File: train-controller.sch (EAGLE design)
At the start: 19 parts, among them IC1 MCP4131, IC2 L272, Q1 2n3906, Q2 2n2222

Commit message: board v2, adding readme and license
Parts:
- removed 5V: M02, custom-parts:M02
- removed BOOST: M03, custom-parts:M03
- removed R6: 1k, SparkFun-Resistors:1KOHM-1/4W-5%(PTH)
- added AUX: M02, custom-parts:M02
- added POW: M03, custom-parts:M03
- CTL: value M02 -> M03; device custom-parts:M02 -> custom-parts:M03
- Q1: value 2n3906 -> BC838
- R2: value 2.7k -> 1k
- SERIAL: value M03 -> M02; device custom-parts:M03 -> custom-parts:M02
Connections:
- removed net 5V-EN: BOOST.P$1, Q1.C
- removed net N$2: IC1.A, R2.1
- new net 12V-EN: AUX.P$1, IC2.V+, Q1.C
- net 12V: now also POW.P$2, Q1.E; no longer BOOST.P$3, IC2.V+
- net 5V: now also IC1.B, POW.P$1; no longer 5V.P$1, Q1.E, R2.2
- net CS: now also CTL.P$1; no longer SERIAL.P$3
- net DIR: now also CTL.P$3, R5.1; no longer CTL.P$2, R6.1
- net EN: now also CTL.P$2, R4.2; no longer CTL.P$1, R5.2
- net GND: now also AUX.P$2, IC1.A, POW.P$3, R3.2; no longer 5V.P$2, BOOST.P$2, IC1.B, R4.2
- net N$1: now also R4.1; no longer R5.1
- net N$3: now also R2.1; no longer R4.1
- net N$6: now also R5.2; no longer R6.2
- net POW: now also R2.2; no longer R3.2
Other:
- moved on the sheet: R2, R3, R4, R5

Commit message: addressing several items from the bug/feature list
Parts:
- removed Q2: 2n2222, custom-parts:TRANSISTOR_NPNTO92
- added D1: (no value), SparkFun-DiscreteSemi:DIODE1N4148
- added Q3: BC638, custom-parts:TRANSISTOR_PNPTO92
- Q1: value BC838 -> BC638
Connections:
- removed net N$5: Q2.C, S1.-
- new net N$2: D1.C, Q3.C, S1.+
- net 12V: now also POW.P$3; no longer POW.P$2
- net 5V: now also Q3.E; no longer S1.+
- net EN: now also R4.1; no longer R4.2
- net GND: now also D1.A, M(V).P$1, POW.P$2, S1.-; no longer M(V).P$2, POW.P$3, Q2.E
- net N$1: now also R4.2; no longer R4.1
- net N$6: now also Q3.B; no longer Q2.B
- net POW: now also M(V).P$2; no longer M(V).P$1
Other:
- moved on the sheet: M(I), M(V), R4, R5

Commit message: adding controller board
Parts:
- R3: value 1k -> -VAR-
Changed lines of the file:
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@@
 <part name="R4" library="SparkFun-Resistors" deviceset="1KOHM-1/4W-5%(PTH)" device="" value="1k"/>
 <part name="R2" library="SparkFun-Resistors" deviceset="1KOHM-1/4W-5%(PTH)" device="" value="1k"/>
-<part name="R3" library="SparkFun-Resistors" deviceset="1KOHM-1/4W-5%(PTH)" device="" value="1k"/>
+<part name="R3" library="SparkFun-Resistors" deviceset="1KOHM-1/4W-5%(PTH)" device="" value="-VAR-"/>
 <part name="R5" library="SparkFun-Resistors" deviceset="1KOHM-1/4W-5%(PTH)" device="" value="1k"/>
 <part name="S1" library="custom-parts" deviceset="EC2-5NU" device="" value="EC2-5NU"/>

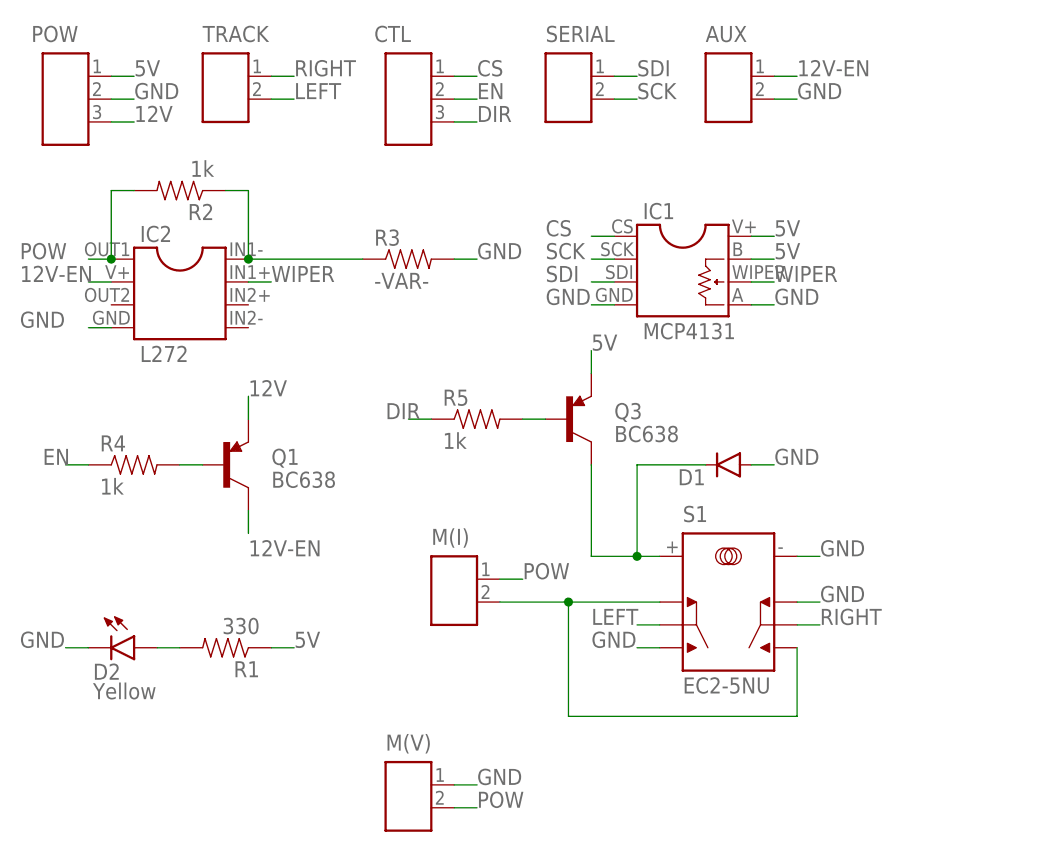
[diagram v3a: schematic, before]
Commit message: getting close to final v2 board, swapping out connectors for molex kk
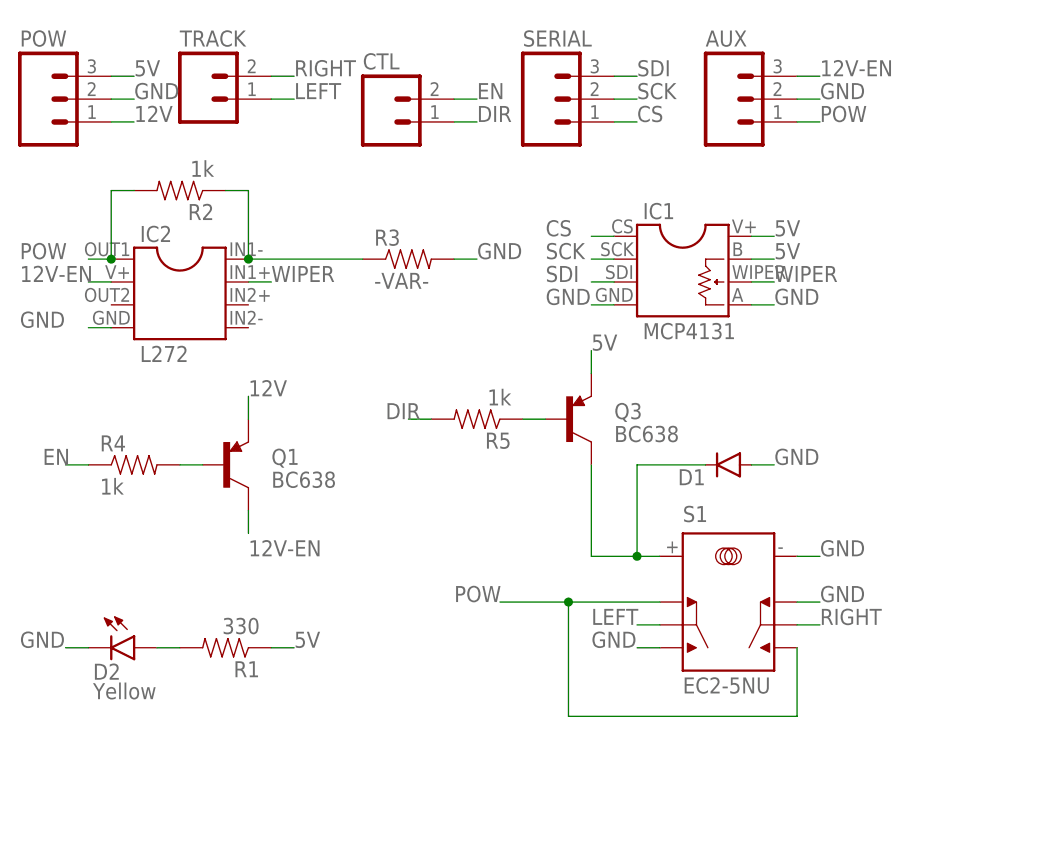
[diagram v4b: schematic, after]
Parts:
- removed M(I), M(V): M02, custom-parts:M02
- AUX, SERIAL: value M02 -> (none); device custom-parts:M02 -> SparkFun-Connectors:M03PTH
- CTL: value M03 -> (none); device custom-parts:M03 -> SparkFun-Connectors:M02PTH
- POW: value M03 -> (none); device custom-parts:M03 -> SparkFun-Connectors:M03PTH
- TRACK: value M02 -> (none); device custom-parts:M02 -> SparkFun-Connectors:M02PTH
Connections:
- removed net N$6: Q3.B, R5.2
- removed net N$7: M(I).P$2, S1.NC1, S1.NO2
- new net N$5: Q3.B, R5.1
- net 12V: now also POW.1; no longer POW.P$3
- net 12V-EN: now also AUX.3; no longer AUX.P$1
- net 5V: now also POW.3; no longer POW.P$1
- net CS: now also SERIAL.1; no longer CTL.P$1
- net DIR: now also CTL.1, R5.2; no longer CTL.P$3, R5.1
- net EN: now also CTL.2; no longer CTL.P$2
- net GND: now also AUX.2, POW.2; no longer AUX.P$2, M(V).P$1, POW.P$2
- net LEFT: now also TRACK.1; no longer TRACK.P$2
- net POW: now also AUX.1, S1.NC1, S1.NO2; no longer M(I).P$1, M(V).P$2
- net RIGHT: now also TRACK.2; no longer TRACK.P$1
- net SCK: now also SERIAL.2; no longer SERIAL.P$2
- net SDI: now also SERIAL.3; no longer SERIAL.P$1
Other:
- moved on the sheet: CTL, R5

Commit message: update version and documentation
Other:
- moved on the sheet: CTL
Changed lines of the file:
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@@
 <instance part="AUX" gate="G$1" x="88.9" y="83.82"/>
 <instance part="SERIAL" gate="G$1" x="68.58" y="83.82"/>
-<instance part="CTL" gate="G$1" x="50.8" y="81.28"/>
+<instance part="CTL" gate="G$1" x="50.8" y="83.82"/>
 </instances>
 <busses>
@@
 <net name="EN" class="0">
 <segment>
-<wire x1="58.42" y1="83.82" x2="60.96" y2="83.82" width="0.1524" layer="91"/>
-<label x="60.96" y="83.82" size="1.778" layer="95"/>
+<wire x1="58.42" y1="86.36" x2="60.96" y2="86.36" width="0.1524" layer="91"/>
+<label x="60.96" y="86.36" size="1.778" layer="95"/>
 <pinref part="CTL" gate="G$1" pin="2"/>
 </segment>
@@
 <net name="DIR" class="0">
 <segment>
-<wire x1="58.42" y1="81.28" x2="60.96" y2="81.28" width="0.1524" layer="91"/>
-<label x="60.96" y="81.28" size="1.778" layer="95"/>
+<wire x1="58.42" y1="83.82" x2="60.96" y2="83.82" width="0.1524" layer="91"/>
+<label x="60.96" y="83.82" size="1.778" layer="95"/>
 <pinref part="CTL" gate="G$1" pin="1"/>
 </segment>
